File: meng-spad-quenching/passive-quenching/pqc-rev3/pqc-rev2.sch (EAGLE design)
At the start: 54 parts, among them IC1 OPA858, IC2 OPA858, IC3 LM8261, IC4 TPS7A4901, Q1 NTR5105P, Q2 BSS123LT1G, Q3 NUD3160LT1G, X1 CONN_SPAD, X2 VIN_PWR, X4 VIN_BIAS, X5 SIGNAL_OUT

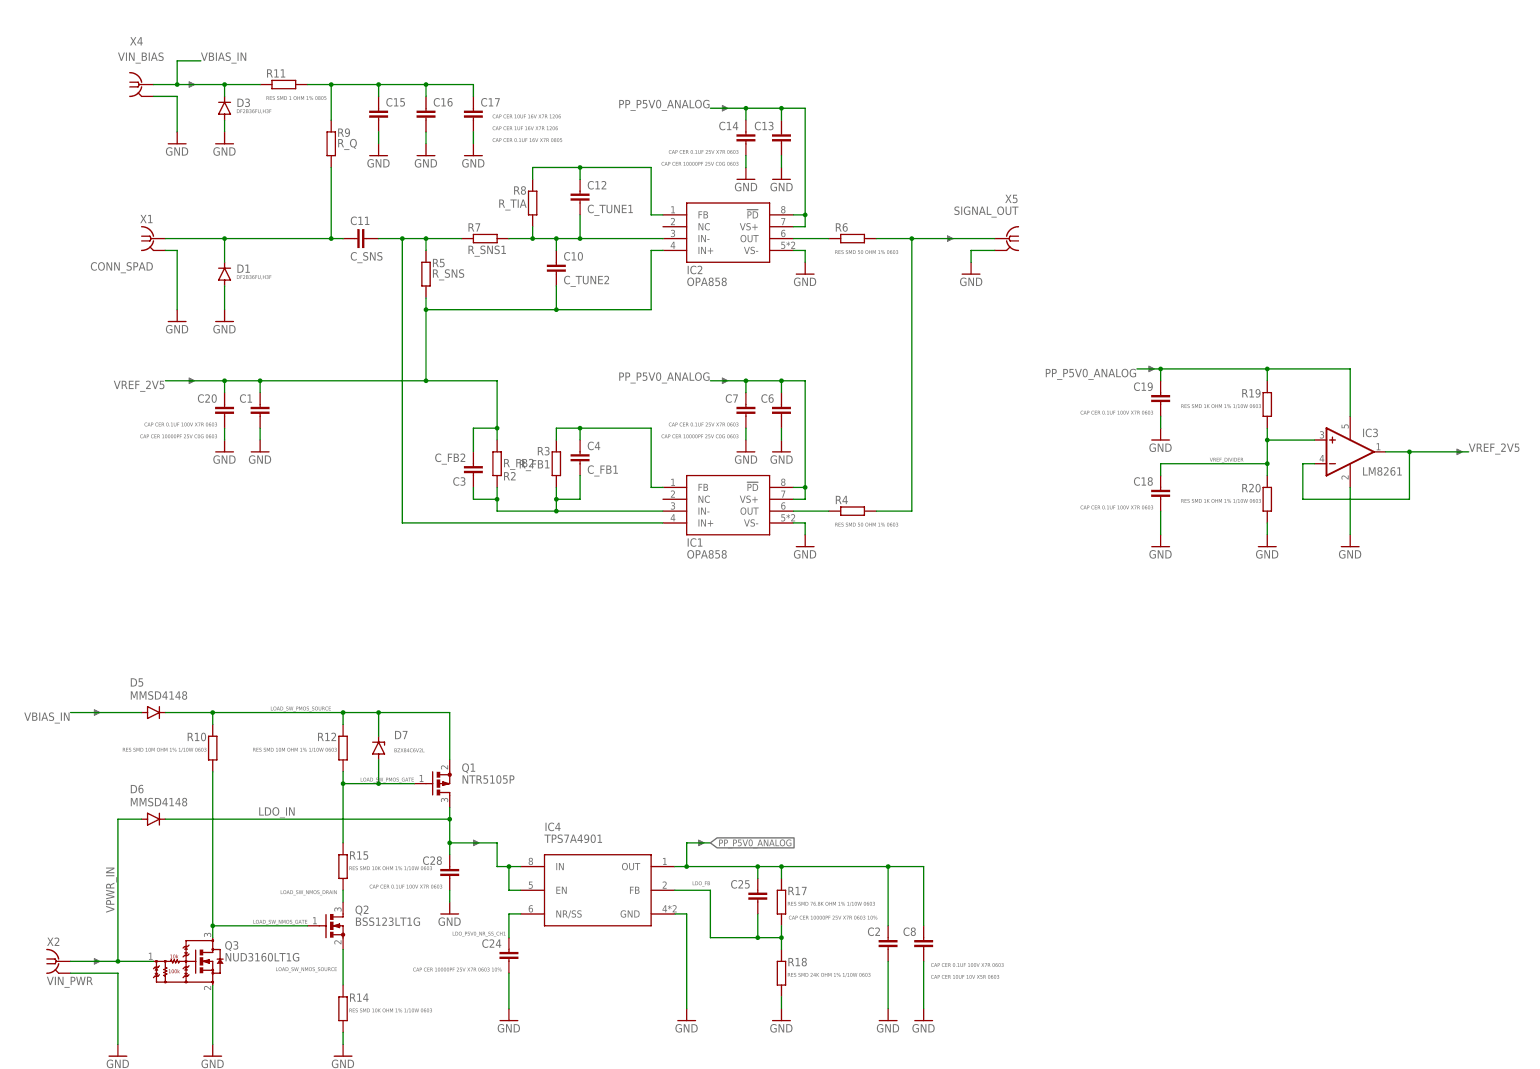
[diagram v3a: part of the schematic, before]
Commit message: Finished layout, renumbered, and exported Gerbers
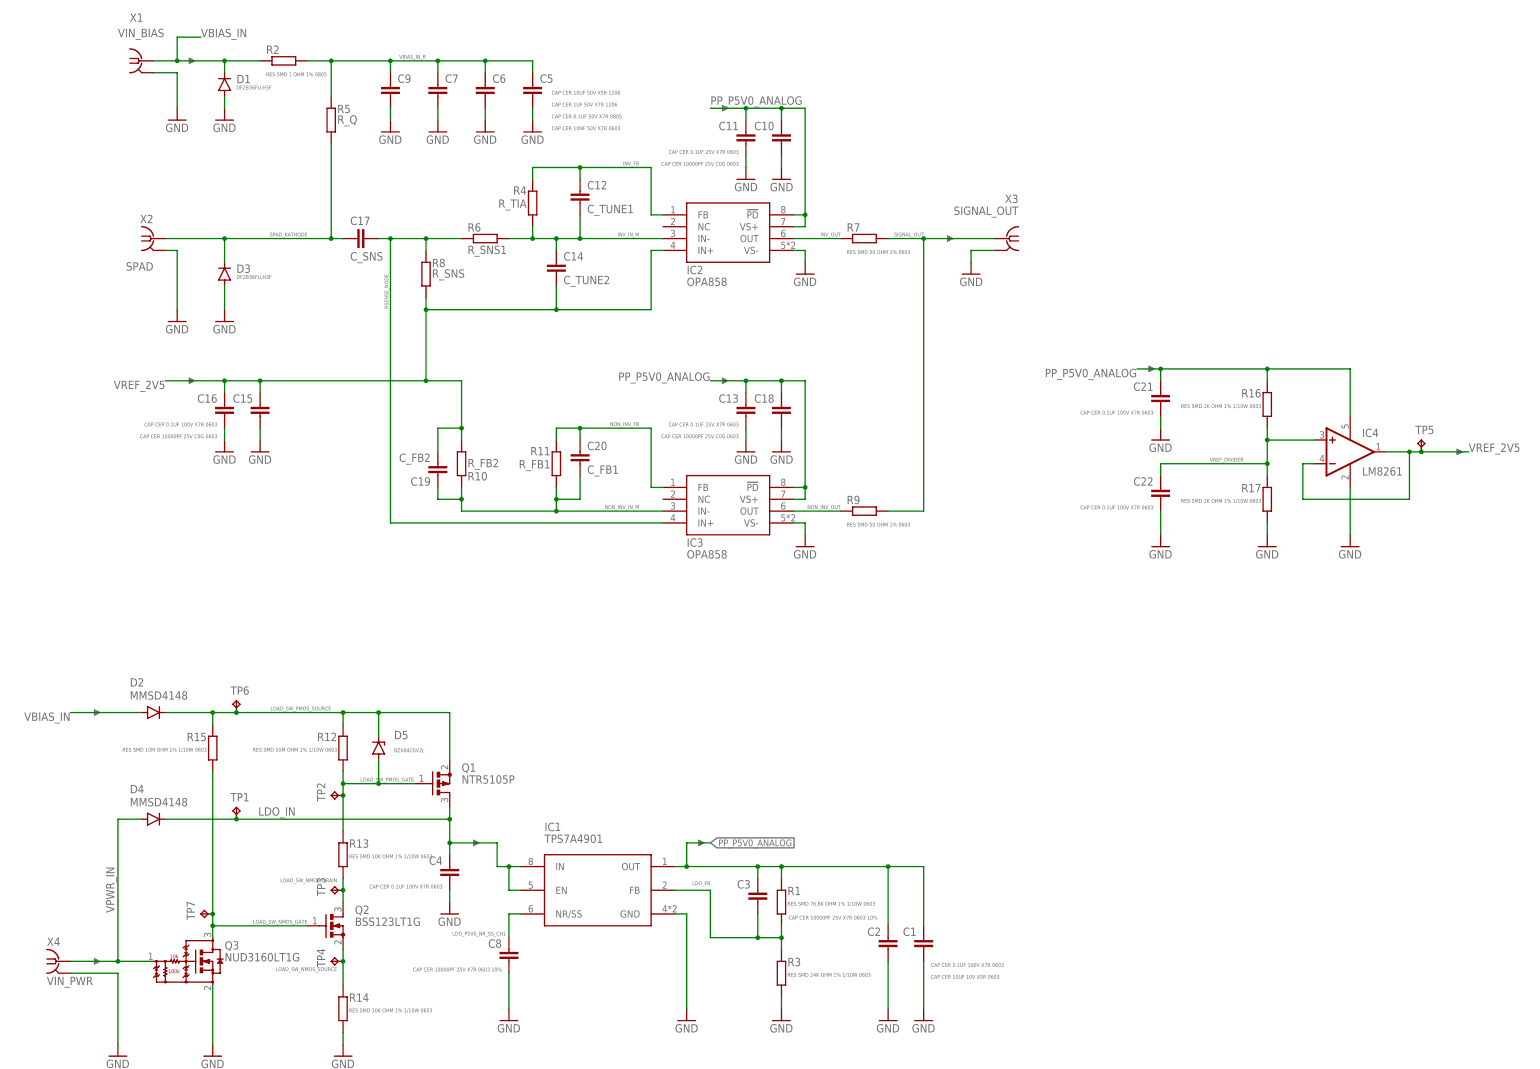
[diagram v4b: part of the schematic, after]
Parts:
- removed C24, C25: CAP CER 10000PF 25V X7R 0603 10%, rcl-modified-footprints:C-EUC0603
- removed C28: CAP CER 0.1UF 100V X7R 0603, rcl-modified-footprints:C-EUC0603
- removed D7: BZX84C6V2L, diode:ZENER-DIODESOT23
- removed R18: RES SMD 24K OHM 1% 1/10W 0603, rcl-modified-footprints:R-EU_R0603
- removed R20: RES SMD 1K OHM 1% 1/10W 0603, rcl-modified-footprints:R-EU_R0603
- added C21, C22: CAP CER 0.1UF 100V X7R 0603, rcl-modified-footprints:C-EUC0603
- added C5: CAP CER 10UF 50V X5R 1206, rcl:C-EUC1206
- added C9: CAP CER 10NF 50V X7R 0603, rcl-modified-footprints:C-EUC0603
- added D2: MMSD4148, diode:DIODE-SOD123
- added R1: RES SMD 76.8K OHM 1% 1/10W 0603, rcl-modified-footprints:R-EU_R0603
- added R13: RES SMD 10K OHM 1% 1/10W 0603, rcl-modified-footprints:R-EU_R0603
- added TP1, TP2, TP3, TP4, TP5, TP6: TPTP10R, testpad:TPTP10R
- added TP7: TPB1,27, testpad:TPB1,27
- C1: value CAP CER 10000PF 25V C0G 0603 -> CAP CER 10UF 10V X5R 0603
- C10: value C_TUNE2 -> CAP CER 10000PF 25V C0G 0603; device rcl-modified-footprints:C-EUC0402 -> rcl-modified-footprints:C-EUC0603
- C11: value C_SNS -> CAP CER 0.1UF 25V X7R 0603
- C13: value CAP CER 10000PF 25V C0G 0603 -> CAP CER 0.1UF 25V X7R 0603
- C14: value CAP CER 0.1UF 25V X7R 0603 -> C_TUNE2; device rcl-modified-footprints:C-EUC0603 -> rcl-modified-footprints:C-EUC0402
- C15: value CAP CER 0.1UF 16V X7R 0805 -> CAP CER 10000PF 25V C0G 0603; device rcl:C-EUC0805 -> rcl-modified-footprints:C-EUC0603
- C16: value CAP CER 1UF 16V X7R 1206 -> CAP CER 0.1UF 100V X7R 0603; device rcl:C-EUC1206 -> rcl-modified-footprints:C-EUC0603
- C17: value CAP CER 10UF 16V X7R 1206 -> C_SNS; device rcl:C-EUC1206 -> rcl-modified-footprints:C-EUC0603
- C18: value CAP CER 0.1UF 100V X7R 0603 -> CAP CER 10000PF 25V C0G 0603
- C19: value CAP CER 0.1UF 100V X7R 0603 -> C_FB2; device rcl-modified-footprints:C-EUC0603 -> rcl-modified-footprints:C-EUC0402
- C20: value CAP CER 0.1UF 100V X7R 0603 -> C_FB1; device rcl-modified-footprints:C-EUC0603 -> rcl-modified-footprints:C-EUC0402
- C3: value C_FB2 -> CAP CER 10000PF 25V X7R 0603 10%; device rcl-modified-footprints:C-EUC0402 -> rcl-modified-footprints:C-EUC0603
- C4: value C_FB1 -> CAP CER 0.1UF 100V X7R 0603; device rcl-modified-footprints:C-EUC0402 -> rcl-modified-footprints:C-EUC0603
- C6: value CAP CER 10000PF 25V C0G 0603 -> CAP CER 1UF 50V X7R 1206; device rcl-modified-footprints:C-EUC0603 -> rcl:C-EUC1206
- C7: value CAP CER 0.1UF 25V X7R 0603 -> CAP CER 0.1UF 50V X7R 0805; device rcl-modified-footprints:C-EUC0603 -> rcl:C-EUC0805
- C8: value CAP CER 10UF 10V X5R 0603 -> CAP CER 10000PF 25V X7R 0603 10%
- D5: value MMSD4148 -> BZX84C6V2L; device diode:DIODE-SOD123 -> diode:ZENER-DIODESOT23
- IC1: value OPA858 -> TPS7A4901; device meng:OPA858 -> Kramnik's Library:TPS7A
- IC3: value LM8261 -> OPA858; device meng:LM8261 -> meng:OPA858
- IC4: value TPS7A4901 -> LM8261; device Kramnik's Library:TPS7A -> meng:LM8261
- R10: value RES SMD 10M OHM 1% 1/10W 0603 -> R_FB2; device rcl-modified-footprints:R-EU_R0603 -> rcl-modified-footprints:R-EU_R0402
- R11: value RES SMD 1 OHM 1% 0805 -> R_FB1; device rcl:R-EU_R0805 -> rcl-modified-footprints:R-EU_R0402
- R15: value RES SMD 10K OHM 1% 1/10W 0603 -> RES SMD 10M OHM 1% 1/10W 0603
- R17: value RES SMD 76.8K OHM 1% 1/10W 0603 -> RES SMD 1K OHM 1% 1/10W 0603
- R2: value R_FB2 -> RES SMD 1 OHM 1% 0805; device rcl-modified-footprints:R-EU_R0402 -> rcl:R-EU_R0805
- R3: value R_FB1 -> RES SMD 24K OHM 1% 1/10W 0603; device rcl-modified-footprints:R-EU_R0402 -> rcl-modified-footprints:R-EU_R0603
- R4: value RES SMD 50 OHM 1% 0603 -> R_TIA; device rcl-modified-footprints:R-EU_R0603 -> rcl-modified-footprints:R-EU_R0402
- R5: value R_SNS -> R_Q; device rcl-modified-footprints:R-EU_R0402 -> rcl:R-EU_R0805
- R6: value RES SMD 50 OHM 1% 0603 -> R_SNS1; device rcl-modified-footprints:R-EU_R0603 -> rcl-modified-footprints:R-EU_R0402
- R7: value R_SNS1 -> RES SMD 50 OHM 1% 0603; device rcl-modified-footprints:R-EU_R0402 -> rcl-modified-footprints:R-EU_R0603
- R8: value R_TIA -> R_SNS
- R9: value R_Q -> RES SMD 50 OHM 1% 0603; device rcl:R-EU_R0603 -> rcl-modified-footprints:R-EU_R0603
- X1: value CONN_SPAD -> VIN_BIAS; device meng:SMA-142-0701-881/886 -> con-samtec:COAX
- X2: value VIN_PWR -> SPAD; device con-samtec:COAX -> meng:SMA-142-0701-881/886
- X4: value VIN_BIAS -> VIN_PWR
- renumbered D6 to D4, R19 to R16, X5 to X3
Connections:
- removed net N$1: C15.1, C16.1, C17.1, R11.1, R9.2
- removed net N$10: C3.1, C4.2, IC1.IN-, R2.1, R3.2
- removed net N$11: C4.1, IC1.FB, R3.1
- removed net N$12: R4.1, R6.1, X3COAX.1
- removed net N$16: IC1.OUT, R4.2
- removed net N$2: C11.1, D1.C, R9.1, X1G1.1
- removed net N$4: C10.1, C12.2, IC2.IN-, R7.1, R8.2
- removed net N$5: C12.1, IC2.FB, R8.1
- removed net N$6: C11.2, IC1.IN+, R5.2, R7.2
- removed net N$7: IC2.OUT, R6.2
- new net INV_FB: C12.1, IC2.FB, R4.1
- new net INV_IN_M: C12.2, C14.1, IC2.IN-, R4.2, R6.1
- new net INV_OUT: IC2.OUT, R7.2
- new net NON_INV_FB: C20.1, IC3.FB, R11.1
- new net NON_INV_IN_M: C19.1, C20.2, IC3.IN-, R10.1, R11.2
- new net NON_INV_OUT: IC3.OUT, R9.2
- new net RSENSE_NODE: C17.2, IC3.IN+, R6.2, R8.2
- new net SIGNAL_OUT: R7.1, R9.1, X3COAX.1
- new net SPAD_KATHODE: C17.1, D3.C, R5.1, X2G1.1
- new net VBIAS_IN_R: C5.1, C6.1, C7.1, C9.1, R2.1, R5.2
- net GND: now also C10.2, C11.2, C21.2, C22.2, C4.2, C5.2, C9.2, IC1.GND, IC3.VS-, IC4.V-, R17.1, R3.2, X1COAX.GND, X2G1.GND; no longer C14.2, C17.2, C19.2, C20.2, C24.2, C28.2, IC1.VS-, IC3.V-, IC4.GND, R18.2, R20.1, X1G1.GND, X2COAX.GND
- net LDO_FB: now also C3.2, IC1.FB, R1.1, R3.1; no longer C25.2, IC4.FB, R17.1, R18.1
- net LDO_IN: now also C4.1, IC1.EN, IC1.IN, TP1.TP; no longer C28.1, IC4.EN, IC4.IN
- net LDO_P5V0_NR_SS_CH1: now also C8.1, IC1.NR/SS; no longer C24.1, IC4.NR/SS
- net LOAD_SW_NMOS_DRAIN: now also R13.1, TP3.TP; no longer R15.1
- net LOAD_SW_NMOS_GATE: now also R15.1, TP7.TP; no longer R10.1
- net LOAD_SW_NMOS_SOURCE: now also TP4.TP
- net LOAD_SW_PMOS_GATE: now also D5.A, R13.2, TP2.TP; no longer D7.A, R15.2
- net LOAD_SW_PMOS_SOURCE: now also D2.C, R15.2, TP6.TP; no longer D7.C, R10.2
- net PP_P5V0_ANALOG: now also C1.1, C10.1, C11.1, C18.1, C21.1, C3.1, IC1.OUT, IC3.!PD, IC3.VS+, IC4.V+, R1.2; no longer C14.1, C19.1, C25.1, C6.1, C7.1, C8.1, IC1.!PD, IC1.VS+, IC3.V+, IC4.OUT, R17.2
- net VBIAS_IN: now also D1.C, D2.A, R2.2, X1COAX.1; no longer D3.C, D5.A, R11.2, X4COAX.1
- net VPWR_IN: now also X4COAX.1; no longer X2COAX.1
- net VREF_2V5: now also C14.2, C15.1, C16.1, C19.2, IC4.-IN, IC4.OUT, R10.2, R8.1, TP5.TP; no longer C1.1, C10.2, C20.1, C3.2, IC3.-IN, IC3.OUT, R2.2, R5.1
- net VREF_DIVIDER: now also C22.1, IC4.+IN, R17.2; no longer C18.1, IC3.+IN, R20.2
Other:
- note removed: "Note: fix voltage ratings!"
- moved on the sheet: C1, C10, C11, C13, C14, C15, C16, C17, C18, C19, C20, C3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
